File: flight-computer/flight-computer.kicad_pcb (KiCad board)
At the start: 4 copper layers, 83.7 x 62.9 mm, 96 parts, among them J1 MicroSD Slot, J2 USB_C_Receptacle_USB2.0_16P, J3 SMA_Coax, J4 Conn_01x02, J5 ARM, Q1 PMOS, Q2 NMOS, SW1 SW_Push, U1 RP2040, U10 LM3671MF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

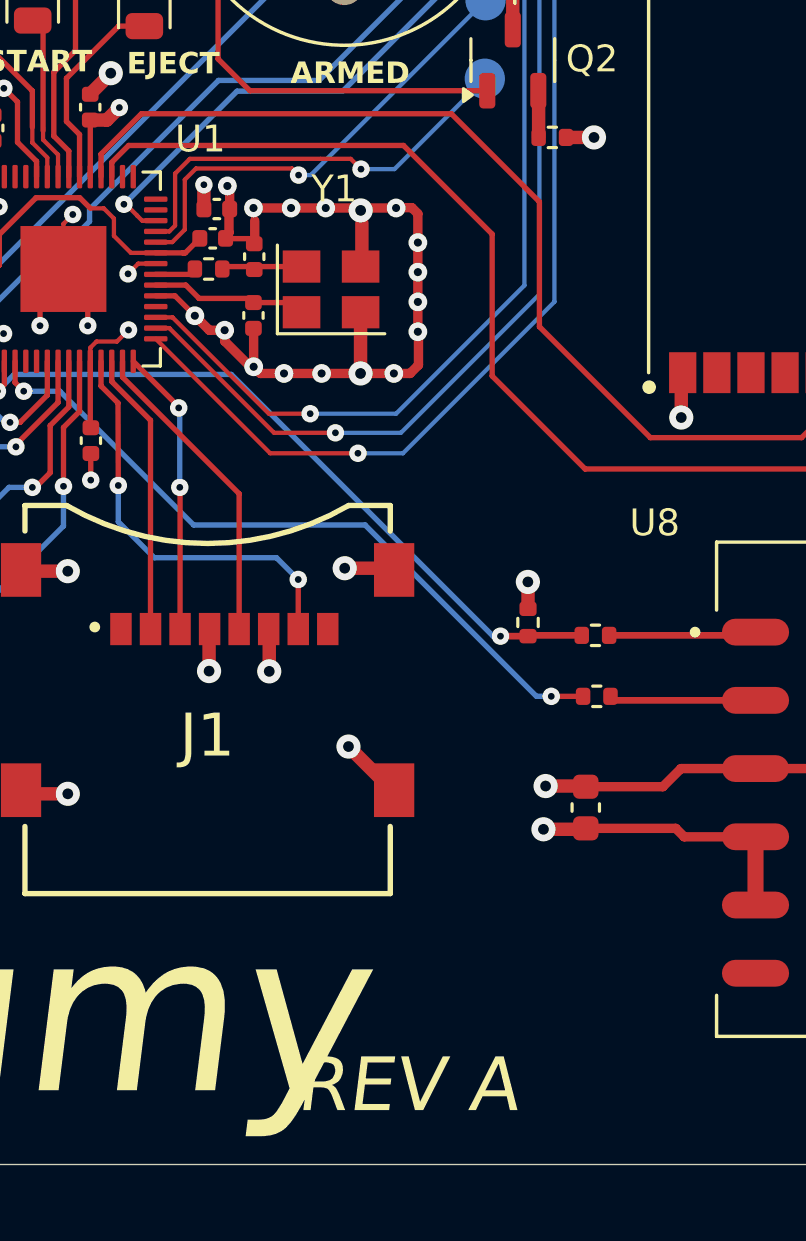
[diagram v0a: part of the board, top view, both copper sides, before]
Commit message: Updated to REV-B; KiCAD's default footprint (or at least first appearing) for the SMD crystal didn't match the datasheet and I didn't catch that. This was the only thing preventing me from booting an otherwise good board. Always check your footprints against the datasheet.
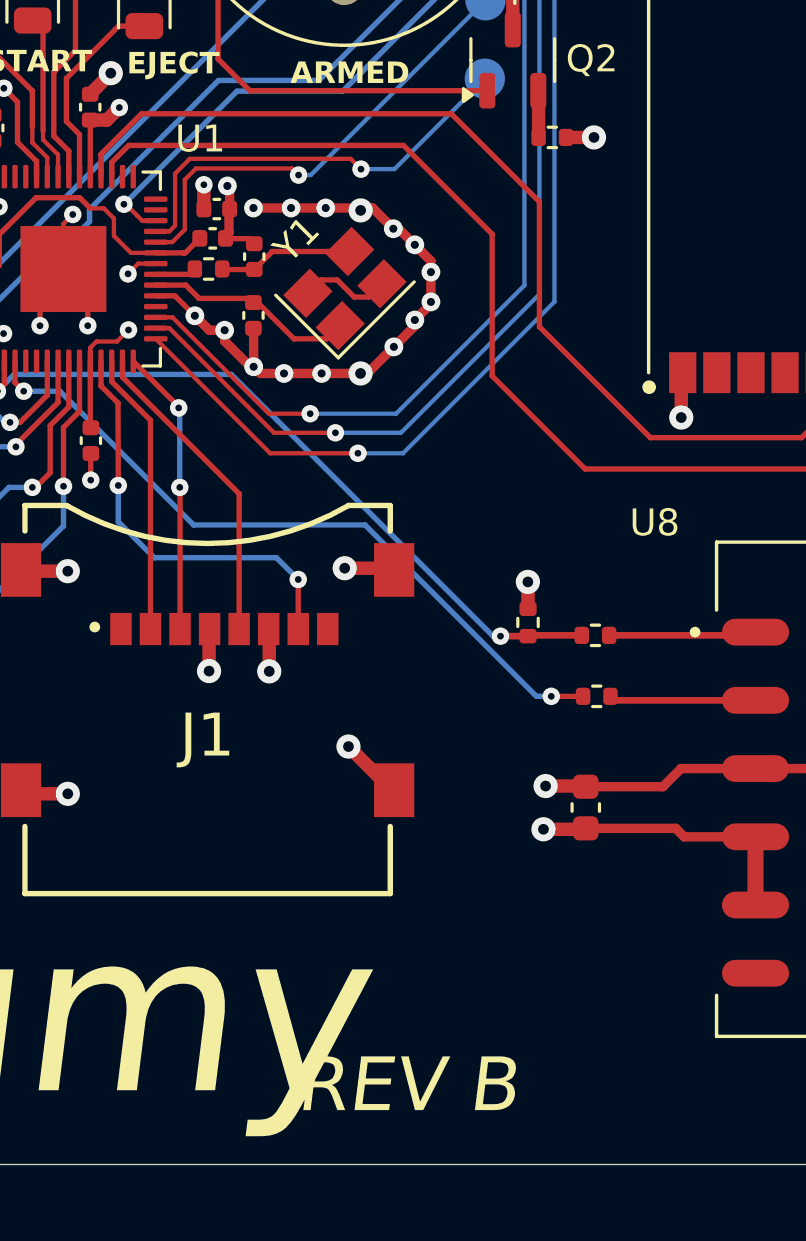
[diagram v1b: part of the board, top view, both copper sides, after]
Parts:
- moved Y1 0.52 mm to (120.7, 100.9), turned to 45 degrees
- renumbered RST to SW2
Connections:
- Y1 pad 3: GND -> Net-(C2-Pad1)
- Y1 pad 4: Net-(C2-Pad1) -> GND
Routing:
- net Net-(C2-Pad1): track 2.99 -> 5.16 mm
- net /XIN: track 5.85 -> 7.90 mm
- net GND: track 299.2 -> 297.1 mm
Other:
- board text added: "REV B"
- board text removed: "REV A"

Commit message: Added silkscreen for magnetometer
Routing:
- net GND: track 297.1 -> 299.1 mm
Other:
- board text added: "IMU"
- board text added: "MAG"
- board text added: "X"
- board text added: "Y"
